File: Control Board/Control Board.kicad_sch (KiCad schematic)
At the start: 72 parts, among them J1 Raspberry_Pi_2_3, Q1 BSS214NH, Q2 BSS214NH, U1 PIC18F16Q41, U2 PI4ULS5V202UEX

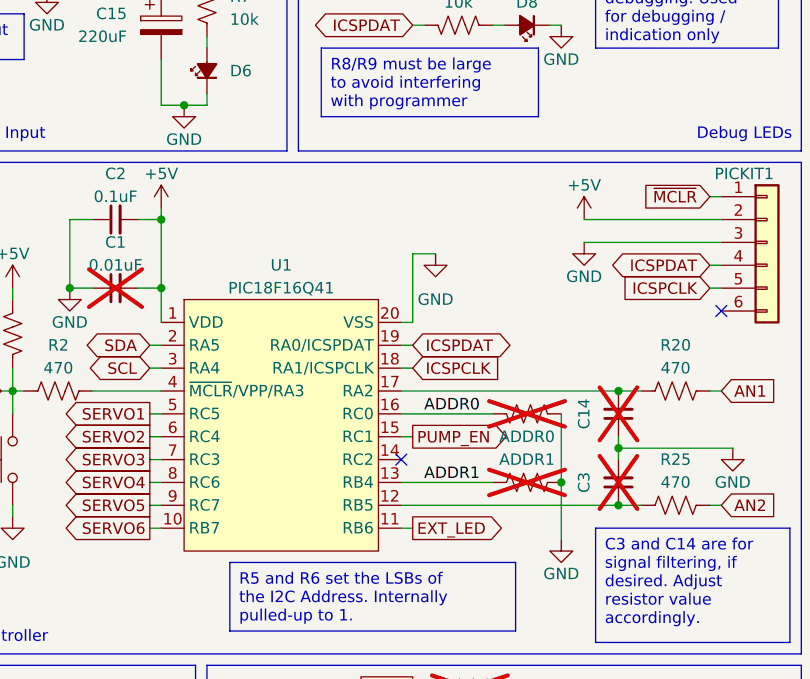
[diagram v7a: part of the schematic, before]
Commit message: Added DAC2 for Self-Testing. Updated PCB/SCH to Rev A2
Increased size of pads for reset switch. Added debug header for OPAMP. Added pin 1 marker for programming.
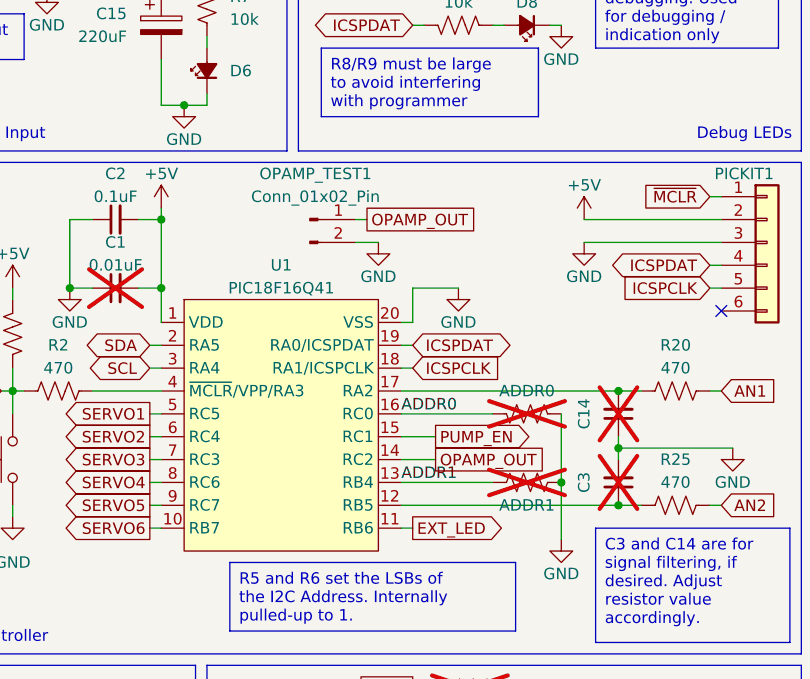
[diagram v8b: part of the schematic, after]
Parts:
- added OPAMP_TEST1: Conn_01x02_Pin, Connector_PinHeader_2.54mm:PinHeader_1x02_P2.54mm_Vertical, symbol Connector:Conn_01x02_Pin
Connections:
- net GND: now also OPAMP_TEST1.2 (Pin_2)
- net OPAMP_OUT: now reaches U1.14 (RC2)
- net OPAMP_OUT: now also OPAMP_TEST1.1 (Pin_1)
- no-connect marks 28 -> 27
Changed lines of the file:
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@@
   (title_block
     (title "Servo Control Board")
-    (date "2023-06-29")
-    (rev "A1")
+    (date "2023-07-20")
+    (rev "A2")
     (company "Designed by: Robert Perkel")
     (comment 1 "https://github.com/robperkel/evilia-boat-servo")
@@
   (no_connect (at 29.21 88.9))
   (no_connect (at 273.05 78.74))
-  (no_connect (at 237.49 95.25))
   (no_connect (at 69.85 86.36))
   (no_connect (at 29.21 91.44))
@@
     (stroke (width 0) (type default))
   )
+  (wire (pts (xy 237.49 95.25) (xy 241.3 95.25))
+    (stroke (width 0) (type default))
+  )
   (wire (pts (xy 109.22 149.86) (xy 109.22 140.97))
     (stroke (width 0) (type default))
@@
     (stroke (width 0) (type default))
   )
+  (wire (pts (xy 232.41 68.58) (xy 233.68 68.58))
+    (stroke (width 0) (type default))
+  )
   (wire (pts (xy 35.56 128.27) (xy 35.56 140.97))
     (stroke (width 0) (type default))
@@
     (stroke (width 0) (type default))
   )
-  (wire (pts (xy 237.49 90.17) (xy 247.65 90.17))
-    (stroke (width 0) (type default))
-  )
   (wire (pts (xy 123.19 60.96) (xy 123.19 66.04))
     (stroke (width 0) (type default))
@@
     (stroke (width 0) (type default))
   )
+  (wire (pts (xy 232.41 71.12) (xy 234.95 71.12))
+    (stroke (width 0) (type default))
+  )
   (wire (pts (xy 104.14 171.45) (xy 106.68 171.45))
     (stroke (width 0) (type default))
@@
     (stroke (width 0) (type default))
   )
+  (wire (pts (xy 237.49 90.17) (xy 247.65 90.17))
+    (stroke (width 0) (type default))
+  )
   (wire (pts (xy 273.05 100.33) (xy 271.78 100.33))
     (stroke (width 0) (type default))
@@
     (stroke (width 0) (type default))
   )
-  (wire (pts (xy 238.76 72.39) (xy 241.3 72.39))
+  (wire (pts (xy 238.76 76.2) (xy 243.84 76.2))
     (stroke (width 0) (type default))
   )
@@
     (stroke (width 0) (type default))
   )
-  (wire (pts (xy 238.76 72.39) (xy 238.76 80.01))
+  (wire (pts (xy 238.76 76.2) (xy 238.76 80.01))
     (stroke (width 0) (type default))
   )
@@
     (stroke (width 0) (type default))
   )
-  (wire (pts (xy 237.49 92.71) (xy 238.76 92.71))
+  (wire (pts (xy 237.49 92.71) (xy 241.3 92.71))
     (stroke (width 0) (type default))
   )
@@
     (effects (font (size 1.27 1.27)) (justify left bottom))
   )
-  (label "ADDR0" (at 240.03 90.17 0) (fields_autoplaced)
+  (label "ADDR0" (at 237.49 90.17 0) (fields_autoplaced)
     (effects (font (size 1.27 1.27)) (justify left bottom))
   )
-  (label "ADDR1" (at 240.03 97.79 0) (fields_autoplaced)
+  (label "ADDR1" (at 237.49 97.79 0) (fields_autoplaced)
     (effects (font (size 1.27 1.27)) (justify left bottom))
   )
@@
     )
   )
+  (global_label "OPAMP_OUT" (shape passive) (at 241.3 95.25 0) (fields_autoplaced)
+    (effects (font (size 1.27 1.27)) (justify left))
+    (property "Intersheetrefs" "${INTERSHEET_REFS}" (at 254.1012 95.25 0)
+      (effects (font (size 1.27 1.27)) (justify left) hide)
+    )
+  )
   (global_label "SERVO6" (shape output) (at 129.54 175.26 0) (fields_autoplaced)
     (effects (font (size 1.27 1.27)) (justify left))
@@
     )
   )
-  (global_label "PUMP_EN" (shape output) (at 238.76 92.71 0) (fields_autoplaced)
+  (global_label "PUMP_EN" (shape output) (at 241.3 92.71 0) (fields_autoplaced)
     (effects (font (size 1.27 1.27)) (justify left))
-    (property "Intersheetrefs" "${INTERSHEET_REFS}" (at 250.4348 92.71 0)
+    (property "Intersheetrefs" "${INTERSHEET_REFS}" (at 252.9748 92.71 0)
       (effects (font (size 1.27 1.27)) (justify left) hide)
     )
@@
     )
   )
+  (global_label "OPAMP_OUT" (shape passive) (at 233.68 68.58 0) (fields_autoplaced)
+    (effects (font (size 1.27 1.27)) (justify left))
+    (property "Intersheetrefs" "${INTERSHEET_REFS}" (at 246.4812 68.58 0)
+      (effects (font (size 1.27 1.27)) (justify left) hide)
+    )
+  )
   (global_label "AN1" (shape input) (at 273.05 87.63 0) (fields_autoplaced)
     (effects (font (size 1.27 1.27)) (justify left))
@@
     )
   )
-  (symbol (lib_id "power:GND") (at 241.3 72.39 0) (unit 1)
-    (in_bom yes) (on_board yes) (dnp no) (fields_autoplaced)
-    (property "Reference" "#PWR01" (at 241.3 78.74 0)
+  (symbol (lib_id "power:GND") (at 243.84 76.2 0) (unit 1)
+    (in_bom yes) (on_board yes) (dnp no)
+    (property "Reference" "#PWR01" (at 243.84 82.55 0)
       (effects (font (size 1.27 1.27)) hide)
     )
-    (property "Value" "GND" (at 241.3 77.47 0)
+    (property "Value" "GND" (at 243.84 80.01 0)
       (effects (font (size 1.27 1.27)))
     )
-    (property "Footprint" "" (at 241.3 72.39 0)
+    (property "Footprint" "" (at 243.84 76.2 0)
       (effects (font (size 1.27 1.27)) hide)
     )
-    (property "Datasheet" "" (at 241.3 72.39 0)
+    (property "Datasheet" "" (at 243.84 76.2 0)
       (effects (font (size 1.27 1.27)) hide)
     )
@@
     )
   )
+  (symbol (lib_id "power:GND") (at 234.95 71.12 0) (unit 1)
+    (in_bom yes) (on_board yes) (dnp no)
+    (property "Reference" "#PWR024" (at 234.95 77.47 0)
+      (effects (font (size 1.27 1.27)) hide)
+    )
+    (property "Value" "GND" (at 234.95 74.93 0)
+      (effects (font (size 1.27 1.27)))
+    )
+    (property "Footprint" "" (at 234.95 71.12 0)
+      (effects (font (size 1.27 1.27)) hide)
+    )
+    (property "Datasheet" "" (at 234.95 71.12 0)
+      (effects (font (size 1.27 1.27)) hide)
+    )
+    (pin "1")
+    (instances
+      (project "Control Board"
+        (path "/f7db5cc7-b482-447d-99b4-42b38c9fd2fd"
+          (reference "#PWR024") (unit 1)
+        )
+      )
+    )
+  )
   (symbol (lib_id "Device:R_US") (at 124.46 138.43 90) (unit 1)
     (in_bom yes) (on_board yes) (dnp no) (fields_autoplaced)
@@
   (symbol (lib_id "Device:R_US") (at 251.46 97.79 90) (unit 1)
     (in_bom yes) (on_board yes) (dnp yes)
-    (property "Reference" "ADDR1" (at 251.46 95.25 90)
+    (property "Reference" "ADDR1" (at 251.46 100.33 90)
       (effects (font (size 1.27 1.27)))
     )
@@
     )
   )
+  (symbol (lib_id "Connector:Conn_01x02_Pin") (at 227.33 68.58 0) (unit 1)
+    (in_bom yes) (on_board yes) (dnp no) (fields_autoplaced)
+    (property "Reference" "OPAMP_TEST1" (at 227.965 63.5 0)
+      (effects (font (size 1.27 1.27)))
+    )
+    (property "Value" "Conn_01x02_Pin" (at 227.965 66.04 0)
+      (effects (font (size 1.27 1.27)))
+    )
+    (property "Footprint" "Connector_PinHeader_2.54mm:PinHeader_1x02_P2.54mm_Vertical" (at 227.33 68.58 0)
+      (effects (font (size 1.27 1.27)) hide)
+    )
+    (property "Datasheet" "~" (at 227.33 68.58 0)
+      (effects (font (size 1.27 1.27)) hide)
+    )
+    (pin "1")
+    (pin "2")
+    (instances
+      (project "Control Board"
+        (path "/f7db5cc7-b482-447d-99b4-42b38c9fd2fd"
+          (reference "OPAMP_TEST1") (unit 1)
+        )
+      )
+    )
+  )
   (symbol (lib_id "Device:C_Small") (at 97.79 38.1 270) (mirror x) (unit 1)
     (in_bom yes) (on_board yes) (dnp no) (fields_autoplaced)
@@
   (symbol (lib_id "Device:R_US") (at 251.46 90.17 90) (mirror x) (unit 1)
     (in_bom yes) (on_board yes) (dnp yes)
-    (property "Reference" "ADDR0" (at 251.46 92.71 90)
+    (property "Reference" "ADDR0" (at 251.46 87.63 90)
       (effects (font (size 1.27 1.27)))
     )
